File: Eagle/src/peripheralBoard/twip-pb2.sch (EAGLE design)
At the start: 31 parts, among them J1 UJ2-BH-1-TH, Q2 IRFD9120

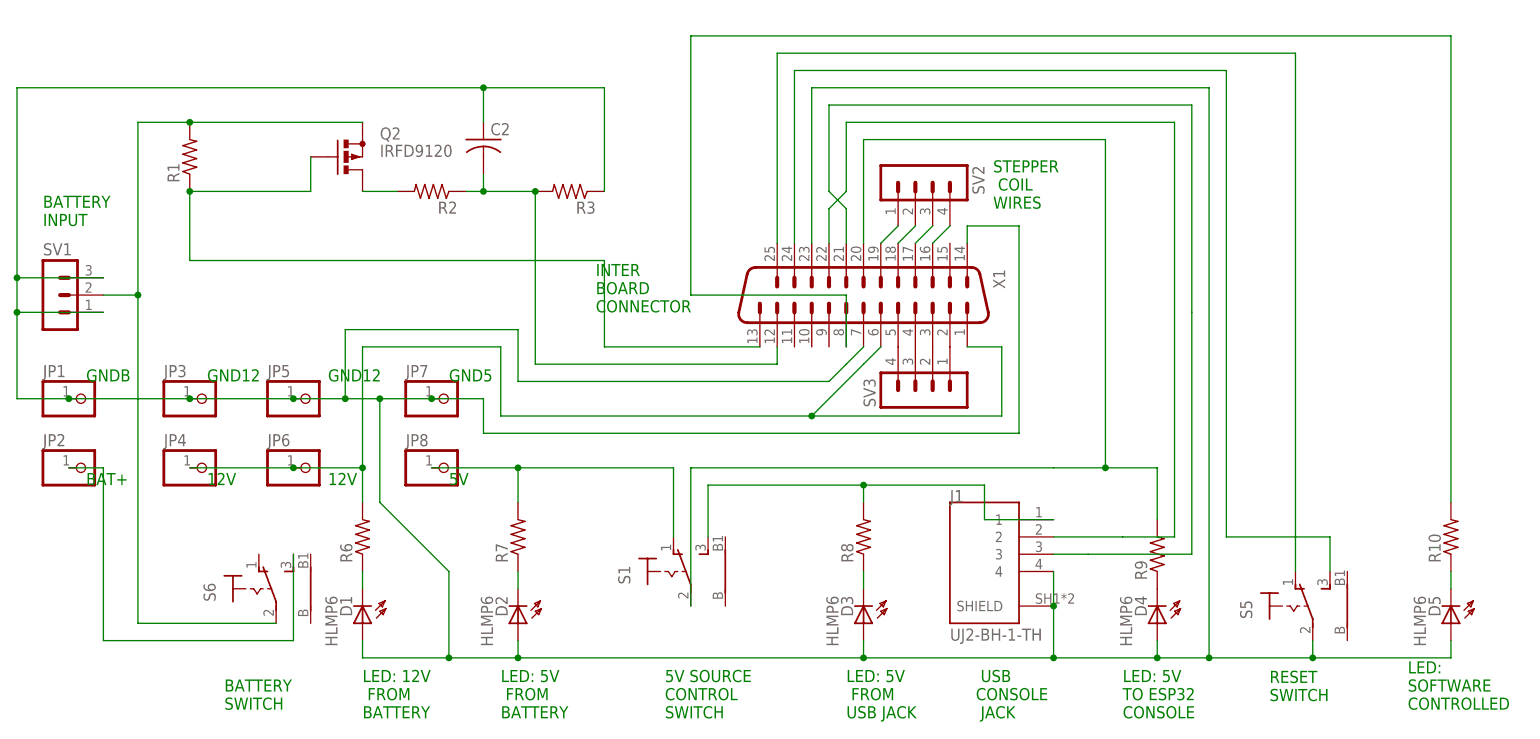
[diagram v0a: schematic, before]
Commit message: Update twip-pb2.sch
 mosfet pullup changes
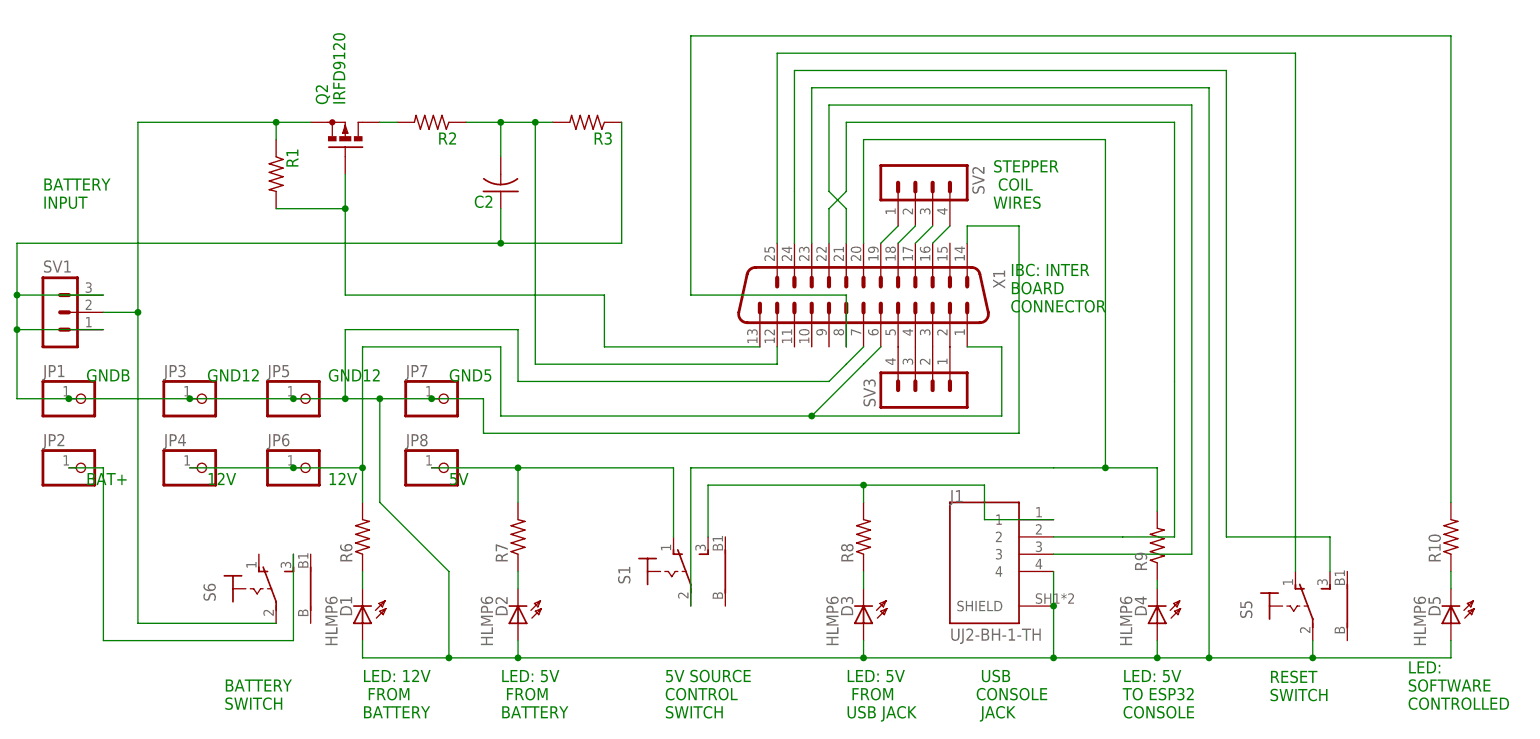
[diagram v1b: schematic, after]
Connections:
- net N$26: now also R1.2; no longer R1.1
- net N$7: now also R1.1; no longer R1.2
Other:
- note added: "IBC: INTER BOARD CONNECTOR"
- note removed: "INTER BOARD CONNECTOR"
- moved on the sheet: C2, Q2, R1, R2, R3, R9, SV1

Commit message: Update twip-pb2.sch
big changes to  IBC pinouts  to  shift stepper connectors around
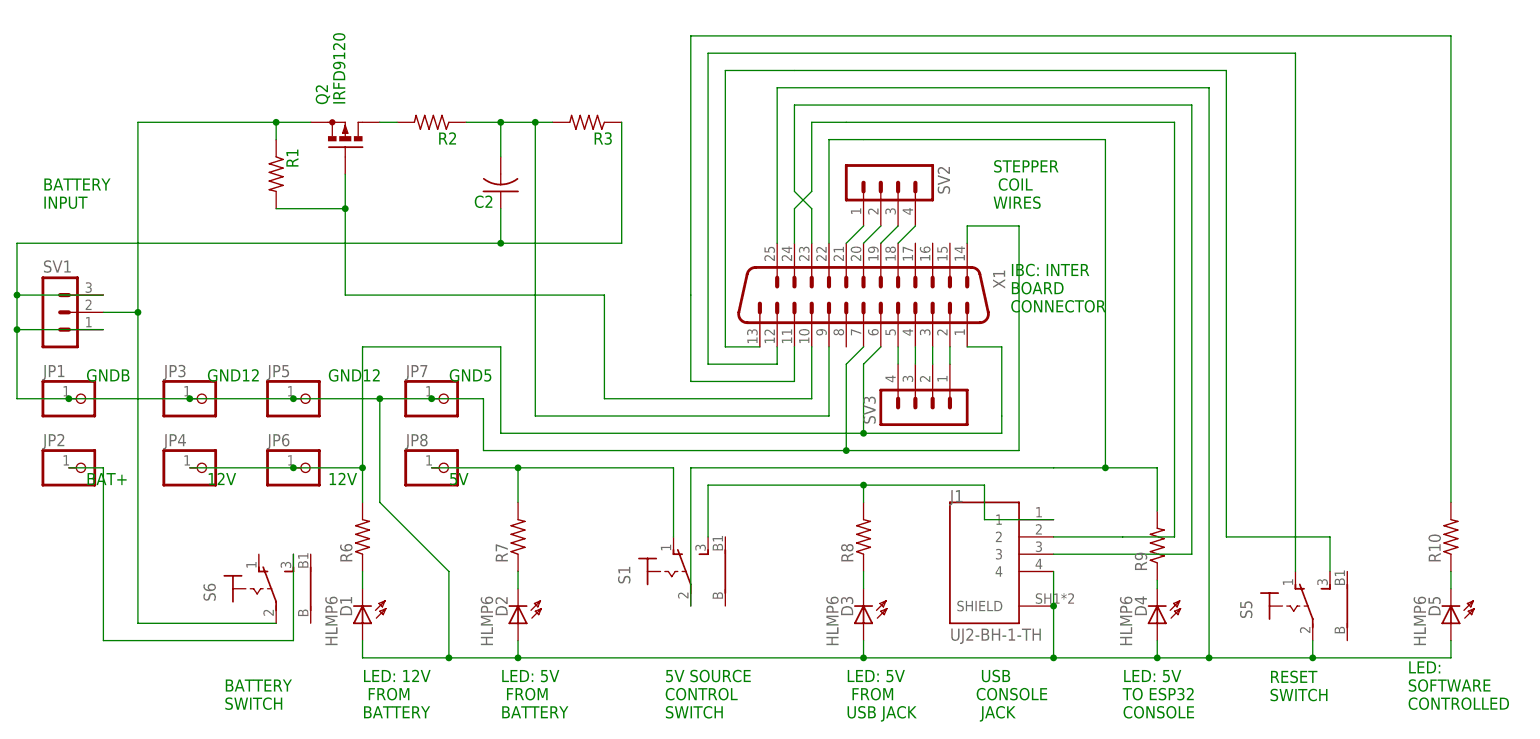
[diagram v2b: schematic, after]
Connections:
- net N$11: now also X1G$1.21; no longer X1G$1.19
- net N$12: now also X1G$1.12; no longer X1G$1.25
- net N$18: now also X1G$1.20; no longer X1G$1.18
- net N$19: now also X1G$1.19; no longer X1G$1.17
- net N$20: now also X1G$1.18; no longer X1G$1.16
- net N$21: now also X1G$1.11; no longer X1G$1.8
- net N$22: now also X1G$1.24; no longer X1G$1.22
- net N$23: now also X1G$1.23; no longer X1G$1.21
- net N$24: now also X1G$1.22; no longer X1G$1.20
- net N$26: now also X1G$1.10; no longer X1G$1.13
- net N$28: now also X1G$1.13; no longer X1G$1.24
- net N$29: now also X1G$1.9; no longer X1G$1.12
- net N$4: now also X1G$1.25; no longer X1G$1.23
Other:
- moved on the sheet: SV2, SV3

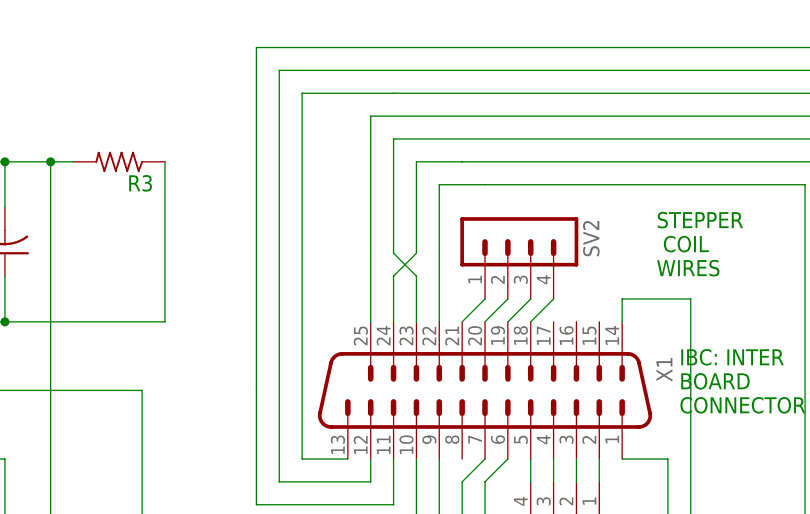
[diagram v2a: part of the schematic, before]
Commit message: Update twip-pb2.sch
fix USB data connections
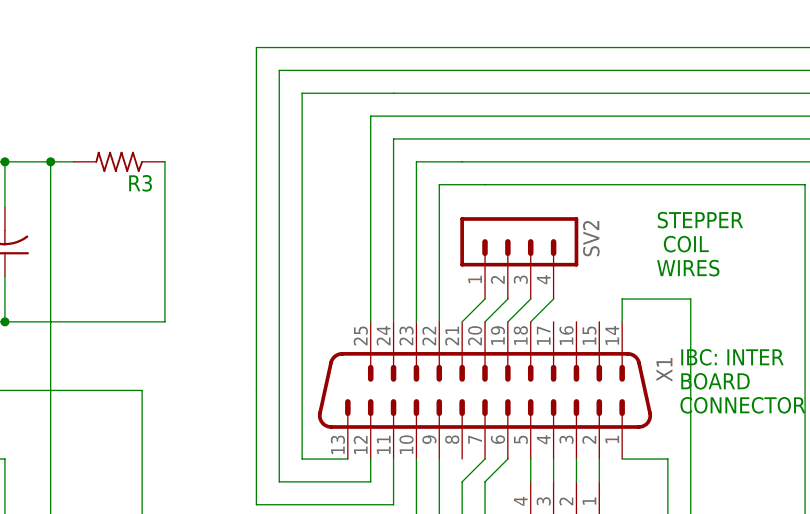
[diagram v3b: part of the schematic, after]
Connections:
- net N$22: now also X1G$1.23; no longer X1G$1.24
- net N$23: now also X1G$1.24; no longer X1G$1.23
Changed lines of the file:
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@@
 <wire x1="99.06" y1="7.62" x2="109.22" y2="7.62" width="0.3048" layer="91"/>
 <wire x1="68.58" y1="68.58" x2="63.5" y2="68.58" width="0.1524" layer="91"/>
-<wire x1="63.5" y1="68.58" x2="63.5" y2="58.42" width="0.1524" layer="91"/>
-<wire x1="63.5" y1="58.42" x2="60.96" y2="55.88" width="0.1524" layer="91"/>
-<pinref part="X1" gate="G$1" pin="24"/>
-<wire x1="60.96" y1="55.88" x2="60.96" y2="50.8" width="0.1524" layer="91"/>
+<pinref part="X1" gate="G$1" pin="23"/>
+<wire x1="63.5" y1="50.8" x2="63.5" y2="68.58" width="0.1524" layer="91"/>
 </segment>
 </net>
 <net name="N$23" class="0">
 <segment>
-<wire x1="60.96" y1="58.42" x2="60.96" y2="71.12" width="0.3048" layer="91"/>
 <wire x1="60.96" y1="71.12" x2="119.38" y2="71.12" width="0.3048" layer="91"/>
 <pinref part="J1" gate="G$1" pin="3"/>
 <wire x1="99.06" y1="5.08" x2="119.38" y2="5.08" width="0.3048" layer="91"/>
 <wire x1="119.38" y1="5.08" x2="119.38" y2="71.12" width="0.3048" layer="91"/>
-<wire x1="63.5" y1="55.88" x2="60.96" y2="58.42" width="0.1524" layer="91"/>
-<pinref part="X1" gate="G$1" pin="23"/>
-<wire x1="63.5" y1="50.8" x2="63.5" y2="55.88" width="0.1524" layer="91"/>
+<pinref part="X1" gate="G$1" pin="24"/>
+<wire x1="60.96" y1="50.8" x2="60.96" y2="71.12" width="0.1524" layer="91"/>
 </segment>
 </net>
